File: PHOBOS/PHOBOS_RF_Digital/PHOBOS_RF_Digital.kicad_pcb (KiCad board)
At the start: 4 copper layers, 167 x 107.5 mm, 20 parts, among them IC1 PD2328J5050S2HF, IC2 PD2328J5050S2HF, IC3 PD2328J5050S2HF, IC4 MAPS-010144-TR0500, IC5 MAPS-010144-TR0500, IC6 MAPS-010144-TR0500, IC7 MAPS-010144-TR0500, J1 RF_IN, J2 PS1, J4 PS2, J5 PS3, J6 PS4, J7 PWR

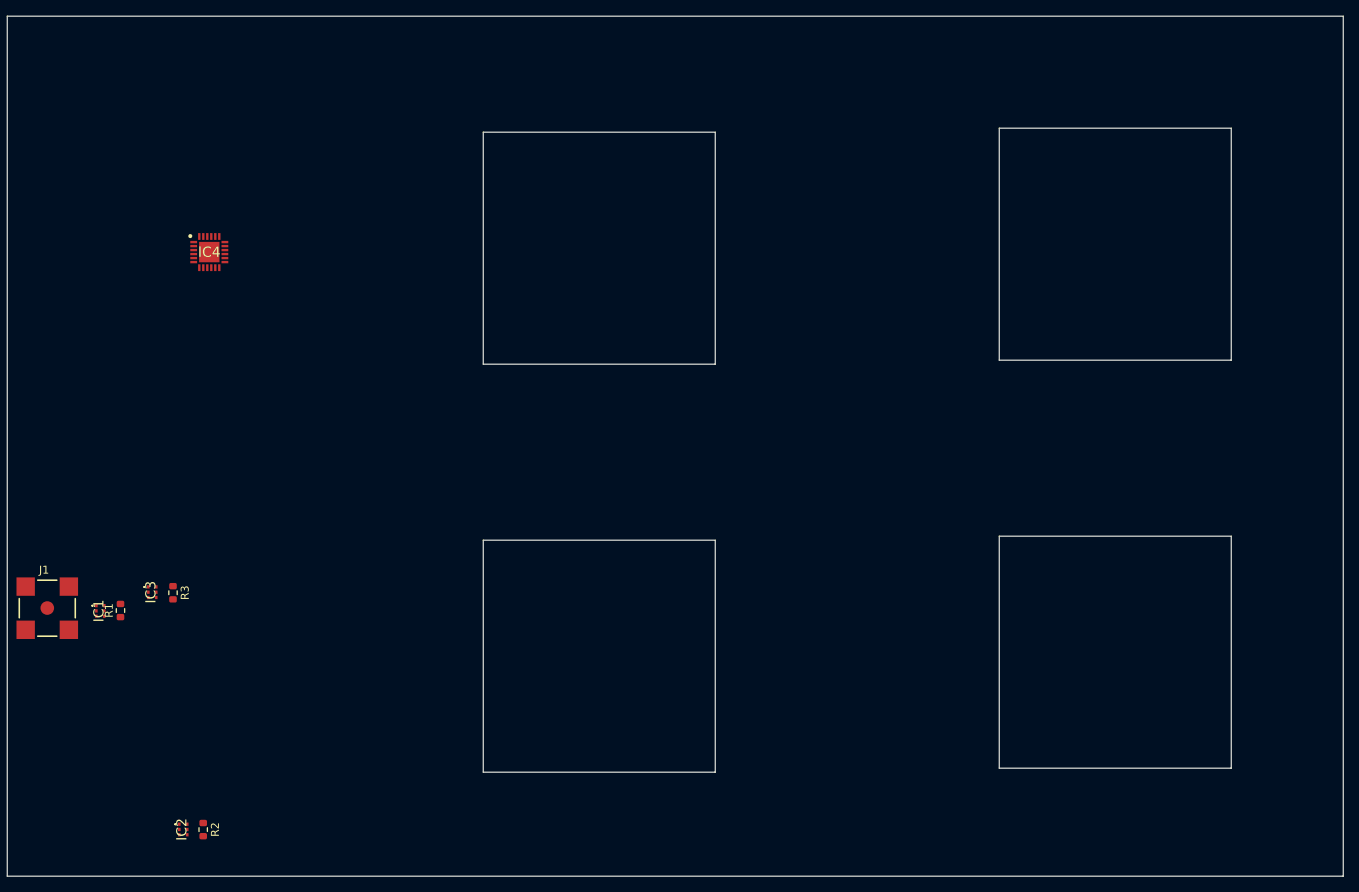
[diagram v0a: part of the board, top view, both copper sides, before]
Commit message: mounting holes added. 1x4 design began
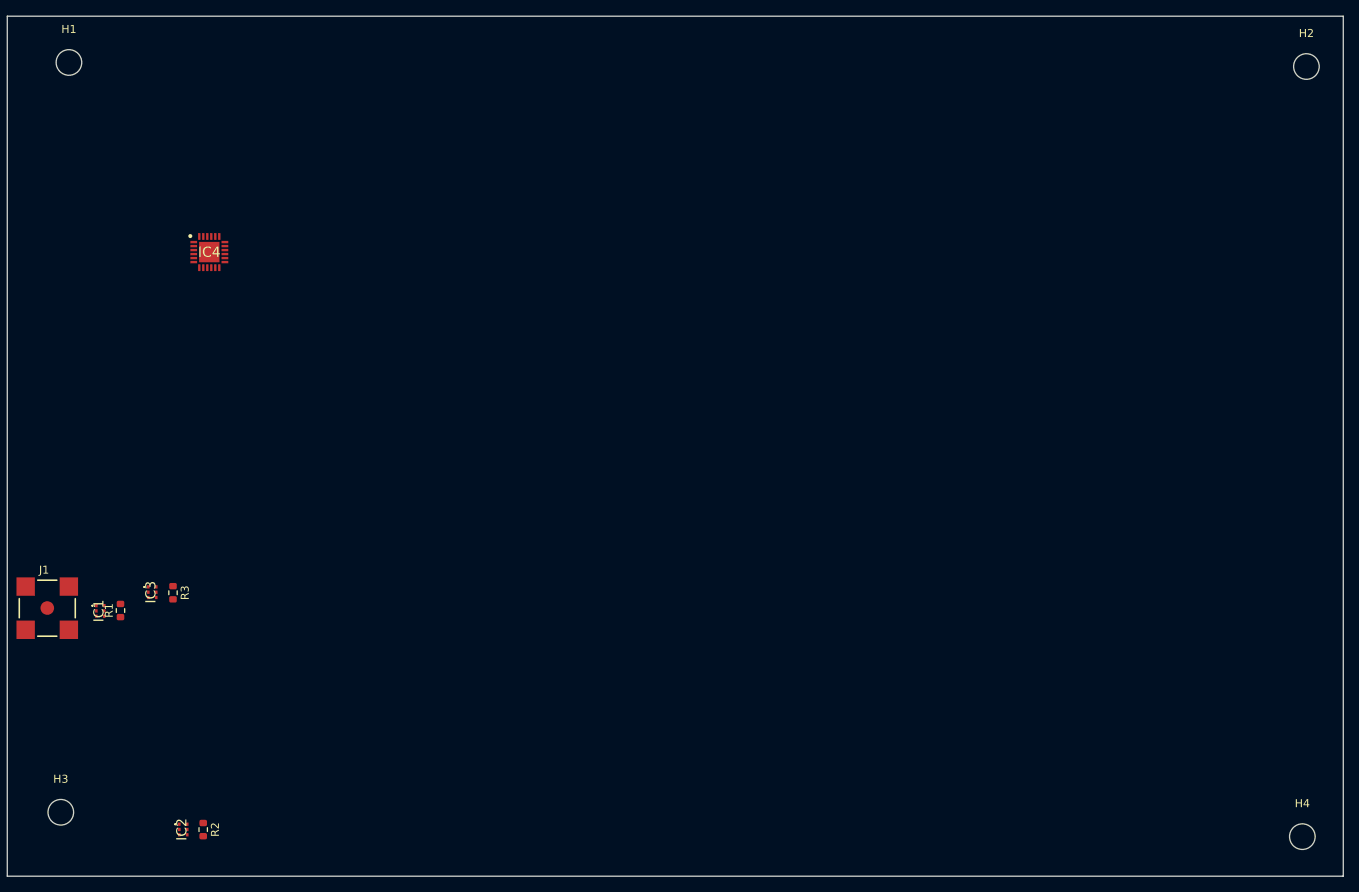
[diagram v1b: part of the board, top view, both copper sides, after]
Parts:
- added H1: MountingHole, MountingHole:MountingHole_3.2mm_M3, F.Cu at (124.2, 33.8)
- added H2: MountingHole, MountingHole:MountingHole_3.2mm_M3, F.Cu at (278.9, 34.3)
- added H3: MountingHole, MountingHole:MountingHole_3.2mm_M3, F.Cu at (123.2, 127.5)
- added H4: MountingHole, MountingHole:MountingHole_3.2mm_M3, F.Cu at (278.4, 130.6)
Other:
- outline, holes or cut-outs redrawn

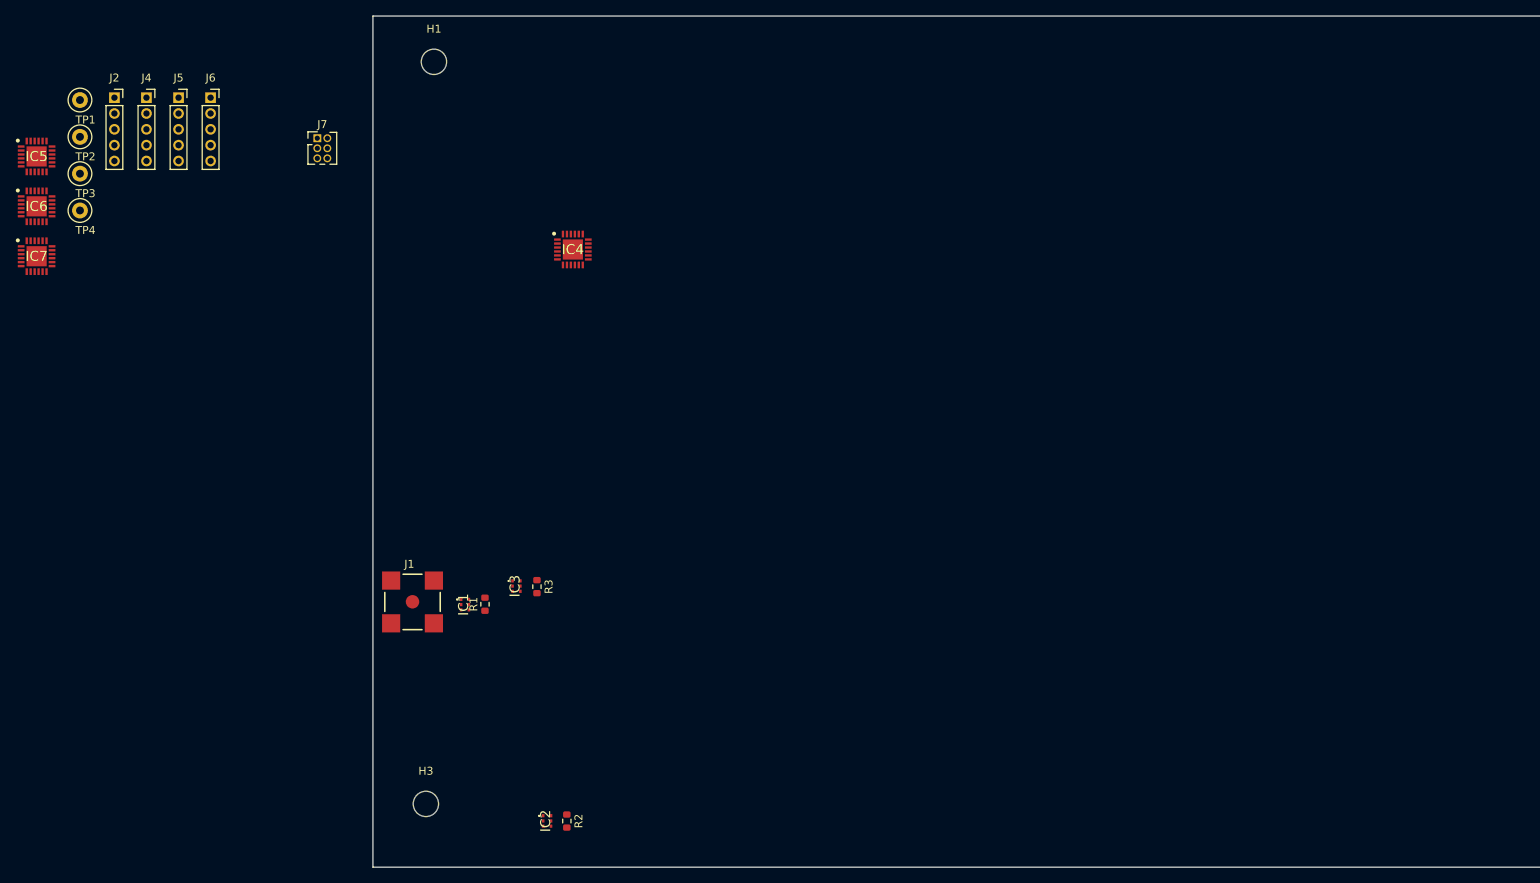
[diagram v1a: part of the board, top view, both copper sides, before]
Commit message: coaxial option layed out for a feel. UPDATE BOARD STACKUP and UPDATE CABLING PLAN
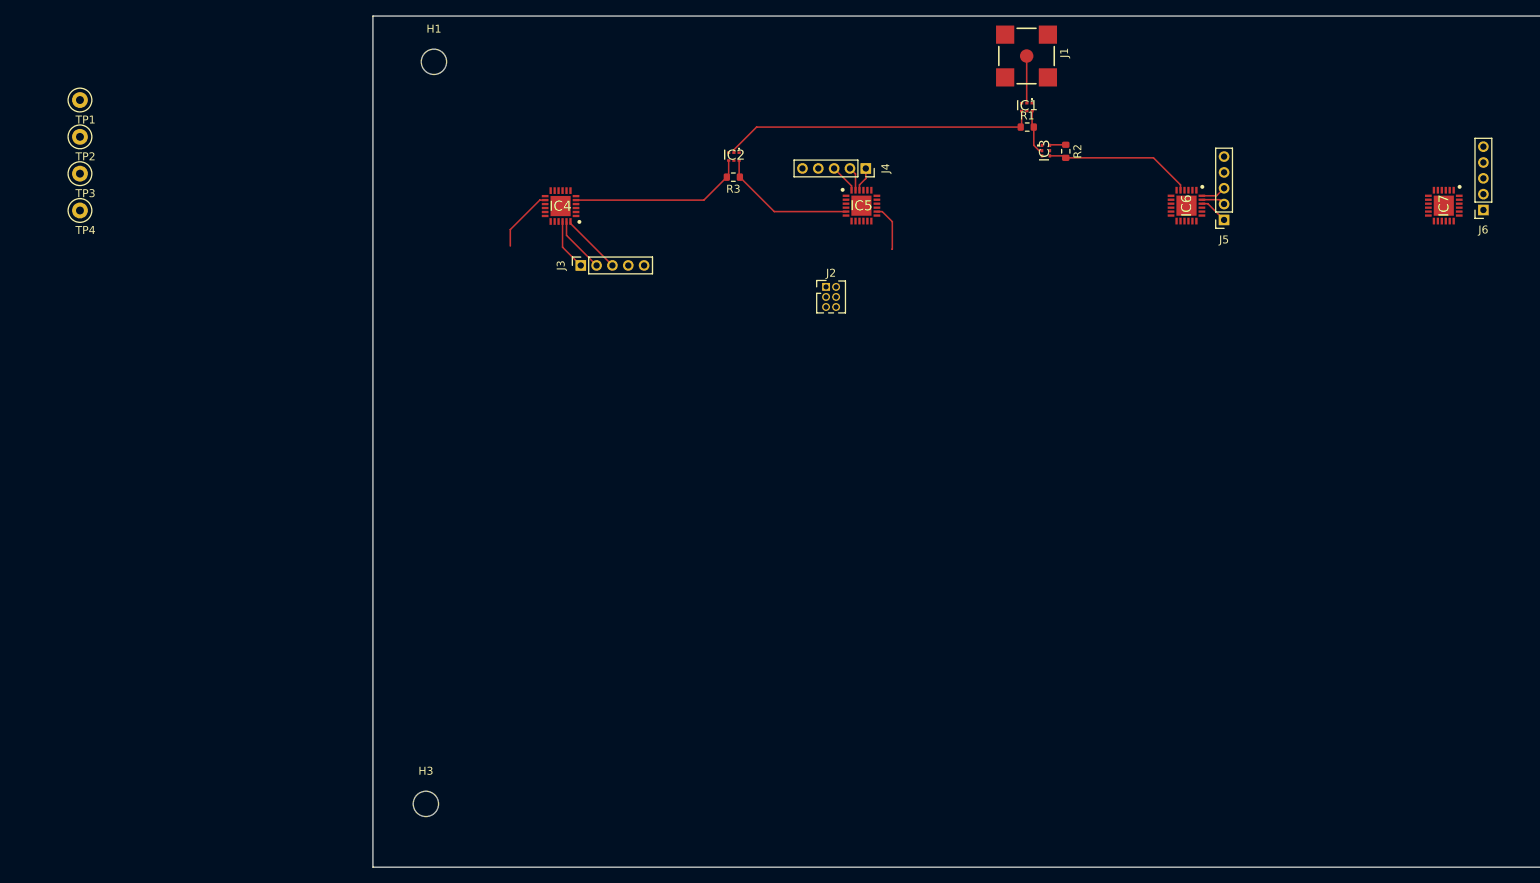
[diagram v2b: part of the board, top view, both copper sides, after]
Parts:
- removed J7: PWR, Connector_PinHeader_1.27mm:PinHeader_2x03_P1.27mm_Vertical
- added J3: PS1, Connector_PinSocket_2.00mm:PinSocket_1x05_P2.00mm_Vertical, F.Cu at (142.8, 59.5)
- J2: value PS1 -> PWR; footprint Connector_PinSocket_2.00mm:PinSocket_1x05_P2.00mm_Vertical -> Connector_PinHeader_1.27mm:PinHeader_2x03_P1.27mm_Vertical
- moved IC7 177.8 mm to (251.8, 52.0), turned to -90 degrees
- moved J6 161.4 mm to (256.8, 52.5), turned to 180 degrees
- moved IC6 145.2 mm to (219.2, 52.0), turned to -90 degrees
- moved J5 133.0 mm to (224.0, 53.8), turned to 180 degrees
- moved R2 105.5 mm to (204.0, 45.1)
- moved IC5 104.4 mm to (178.2, 52.0)
- moved J1 103.8 mm to (199.1, 33.0), turned to -90 degrees
- moved IC1 94.8 mm to (199.1, 39.5), turned to 0 degrees
- moved J2 93.0 mm to (173.7, 62.2)
- moved J4 91.3 mm to (178.8, 47.2), turned to -90 degrees
- moved R1 91.2 mm to (199.1, 42.0), turned to 0 degrees
- moved IC2 87.2 mm to (162.1, 45.8), turned to 0 degrees
- moved IC3 86.6 mm to (201.5, 45.0)
- moved R3 57.4 mm to (162.0, 48.4), turned to 0 degrees
- moved IC4 5.70 mm to (140.2, 52.0), turned to 180 degrees
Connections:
- net Net-(IC5-SER_OUT) renamed /SER_OUT
- J2 pad 1: /LE1 -> +3V3
- J2 pad 2: /SCK_1 -> +3V3
- J2 pad 3: /MOSI_1 -> -3V3
- J2 pad 4: GND -> -3V3
- R2 pad 1: /PORT1 -> /PORT3
- R2 pad 2: /PORT2 -> /PORT4
- R3 pad 1: /PORT3 -> /PORT1
- R3 pad 2: /PORT4 -> /PORT2
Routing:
- net /S1_OUT1: track 0.00 -> 39.8 mm
- net /PORT1: track 0.00 -> 22.4 mm
- net /PORT3: track 0.00 -> 18.7 mm
- net /PORT2: track 0.00 -> 17.4 mm
- net /ANT1: track 0.00 -> 14.0 mm
- net /MOSI_1: track 0.00 -> 7.75 mm
- net /SCK_1: track 0.00 -> 7.12 mm
- net /LE1: track 0.00 -> 6.50 mm
- net /RF_IN: track 0.00 -> 5.97 mm
- net /S1_OUT2: track 0.00 -> 5.73 mm
- net /MOSI_2: track 0.00 -> 3.66 mm
- net /LE3: track 0.00 -> 3.65 mm
- net /MOSI_3: track 0.00 -> 3.19 mm
- net /LE2: track 0.00 -> 3.08 mm
- net /SCK_2: track 0.00 -> 3.04 mm
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
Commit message: 4 SMA version started.
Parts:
- removed J2: PWR, Connector_PinHeader_1.27mm:PinHeader_2x03_P1.27mm_Vertical
- IC1, IC2, IC3, IC4, IC5, IC6, IC7, J1, R1: moved to B.Cu
- J3: value PS1 -> PS2; footprint Connector_PinSocket_2.00mm:PinSocket_1x05_P2.00mm_Vertical -> Connector_PinHeader_1.00mm:PinHeader_2x04_P1.00mm_Vertical; moved to B.Cu
- J4: value PS2 -> PS1; footprint Connector_PinSocket_2.00mm:PinSocket_1x05_P2.00mm_Vertical -> Connector_PinHeader_1.00mm:PinHeader_2x04_P1.00mm_Vertical; moved to B.Cu
- J5, J6: footprint Connector_PinSocket_2.00mm:PinSocket_1x05_P2.00mm_Vertical -> Connector_PinHeader_1.00mm:PinHeader_2x04_P1.00mm_Vertical; moved to B.Cu
- R2: renamed from R3; moved to B.Cu
- R3: renamed from R2; moved to B.Cu
- moved J6 205.7 mm to (51.1, 58.0), turned to -90 degrees
- moved IC7 196.0 mm to (56.1, 63.0)
- moved TP1 172.9 mm to (252.3, 43.2)
- moved J5 115.0 mm to (109.1, 58.1), turned to -90 degrees
- moved IC4 106.6 mm to (246.6, 58.8), turned to 0 degrees
- moved IC6 105.8 mm to (114.1, 63.0)
- moved TP2 96.8 mm to (176.3, 43.0)
- moved H1 94.3 mm to (30.6, 44.8)
- moved H2 93.4 mm to (29.8, 128.8)
- moved R3 72.0 mm to (132.7, 54.9)
- moved IC3 67.0 mm to (135.2, 54.8)
- moved J4 65.1 mm to (241.8, 63.8), turned to 0 degrees
- moved R1 52.8 mm to (147.7, 54.0), turned to 180 degrees
- moved IC1 52.7 mm to (147.7, 51.5), turned to 180 degrees
- moved J1 52.7 mm to (147.7, 44.8)
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- renumbered H3 to H2, H2 to H3
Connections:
- net /SER_OUT renamed Net-(IC5-SER_OUT)
- J3 pad 1: /LE1 -> +3V3
- J3 pad 2: /SCK_1 -> /LE2
- J3 pad 3: /MOSI_1 -> unconnected-(J3-Pin_3-Pad3)
- J3 pad 4: GND -> /SCK_2
- J3 pad 5: GND -> -3V3
- J4 pad 1: /LE2 -> +3V3
- J4 pad 2: /SCK_2 -> /LE1
- J4 pad 3: /MOSI_2 -> unconnected-(J4-Pin_3-Pad3)
- J4 pad 4: GND -> /SCK_1
- J4 pad 5: GND -> -3V3
- J5 pad 1: /LE3 -> +3V3
- J5 pad 2: /SCK_3 -> /LE3
- J5 pad 3: /MOSI_3 -> unconnected-(J5-Pin_3-Pad3)
- J5 pad 4: GND -> /SCK_3
- J5 pad 5: GND -> -3V3
- J6 pad 1: /LE4 -> +3V3
- J6 pad 2: /SCK_4 -> /LE4
- J6 pad 3: /MOSI_4 -> unconnected-(J6-Pin_3-Pad3)
- J6 pad 4: GND -> /SCK_4
- J6 pad 5: GND -> -3V3
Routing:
- net /S1_OUT1: track 39.8 -> 0.00 mm
- net +3V3: track 0.00 -> 34.8 mm
- net -3V3: track 0.00 -> 22.6 mm
- net /PORT1: track 22.4 -> 2.20 mm
- net /PORT2: track 17.4 -> 0.00 mm
- net /PORT3: track 18.7 -> 2.11 mm
- net /ANT1: track 14.0 -> 0.00 mm
- net /RF_IN: track 5.97 -> 0.00 mm
- net /LE4: track 0.00 -> 5.40 mm
- net /MOSI_1: track 7.75 -> 2.98 mm
- net /SCK_4: track 0.00 -> 4.44 mm
- net /S1_OUT2: track 5.73 -> 1.32 mm
- net GND: track 0.00 -> 4.19 mm
- net /MOSI_4: track 0.00 -> 3.13 mm
- net /SCK_1: track 7.12 -> 4.19 mm
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- added copper zone on In1.Cu, net GND
- added copper zone on In2.Cu, net GND
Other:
- board size 167 x 107.5 mm -> 251.2 x 96.5 mm
